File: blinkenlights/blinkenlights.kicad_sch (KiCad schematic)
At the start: 9 parts, among them U101 ATF22V10C, U102 SST39SF020, U103 SST39SF020

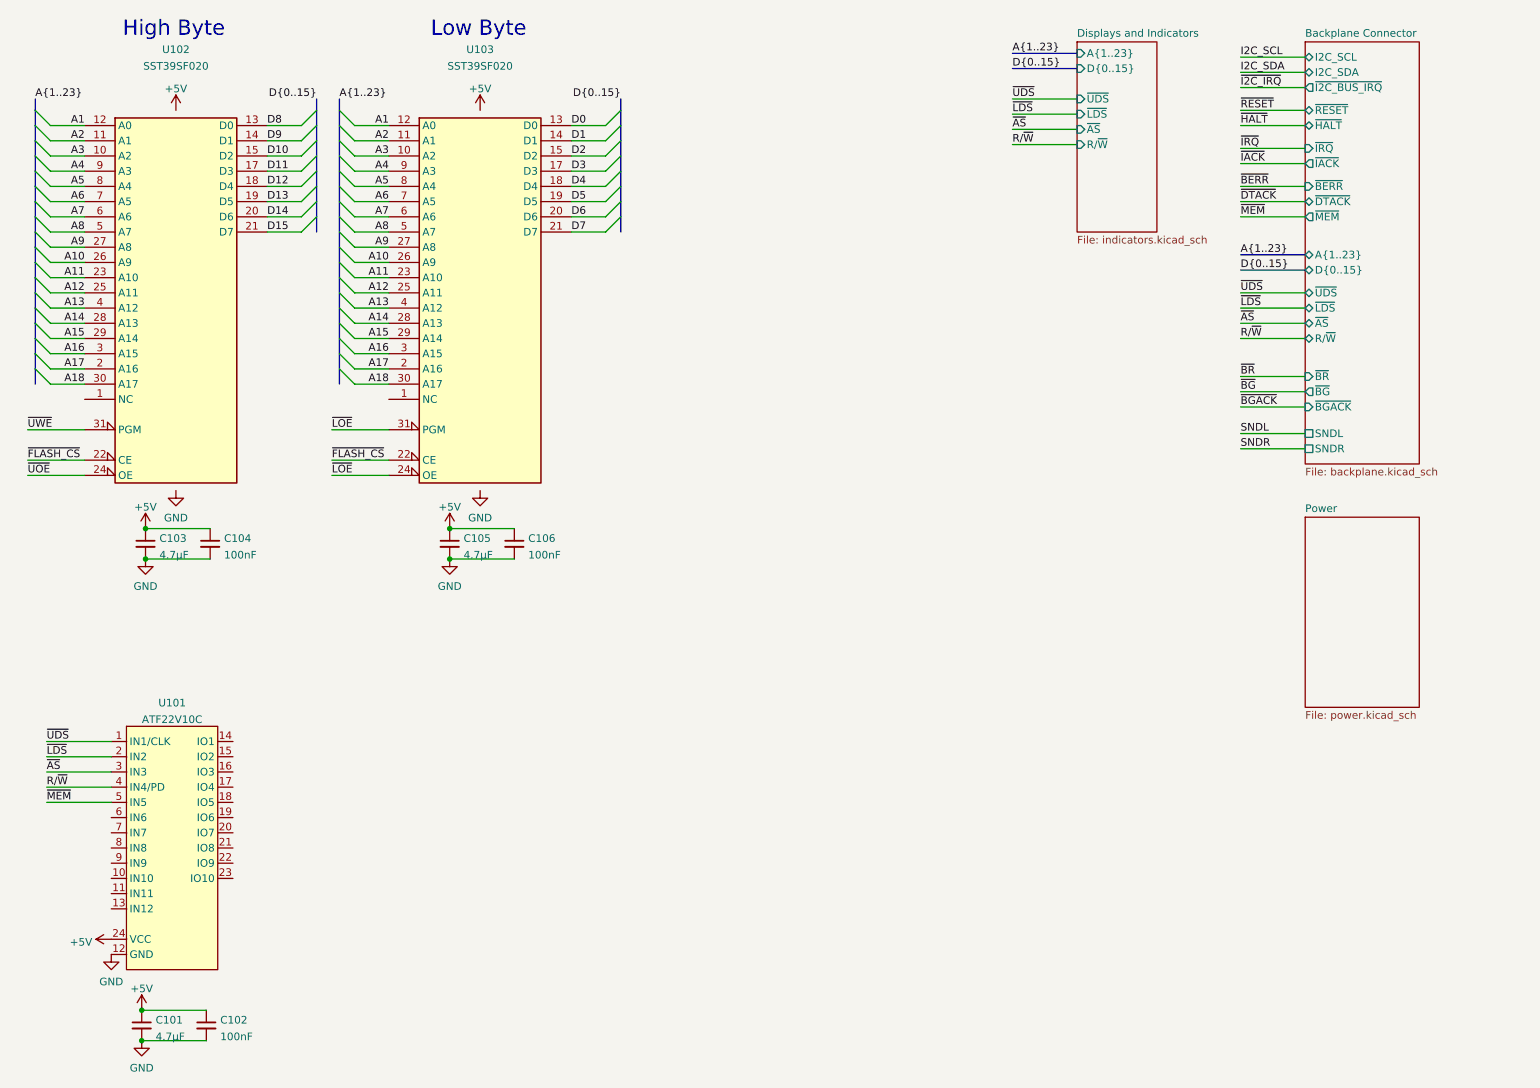
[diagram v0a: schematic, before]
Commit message: Start work on blinkenlights pcb
- This is mostly for the general layout and physical size of the board;
  all the components are placed on the back so the pin numbers will line
  up properly on the DIN connectors.
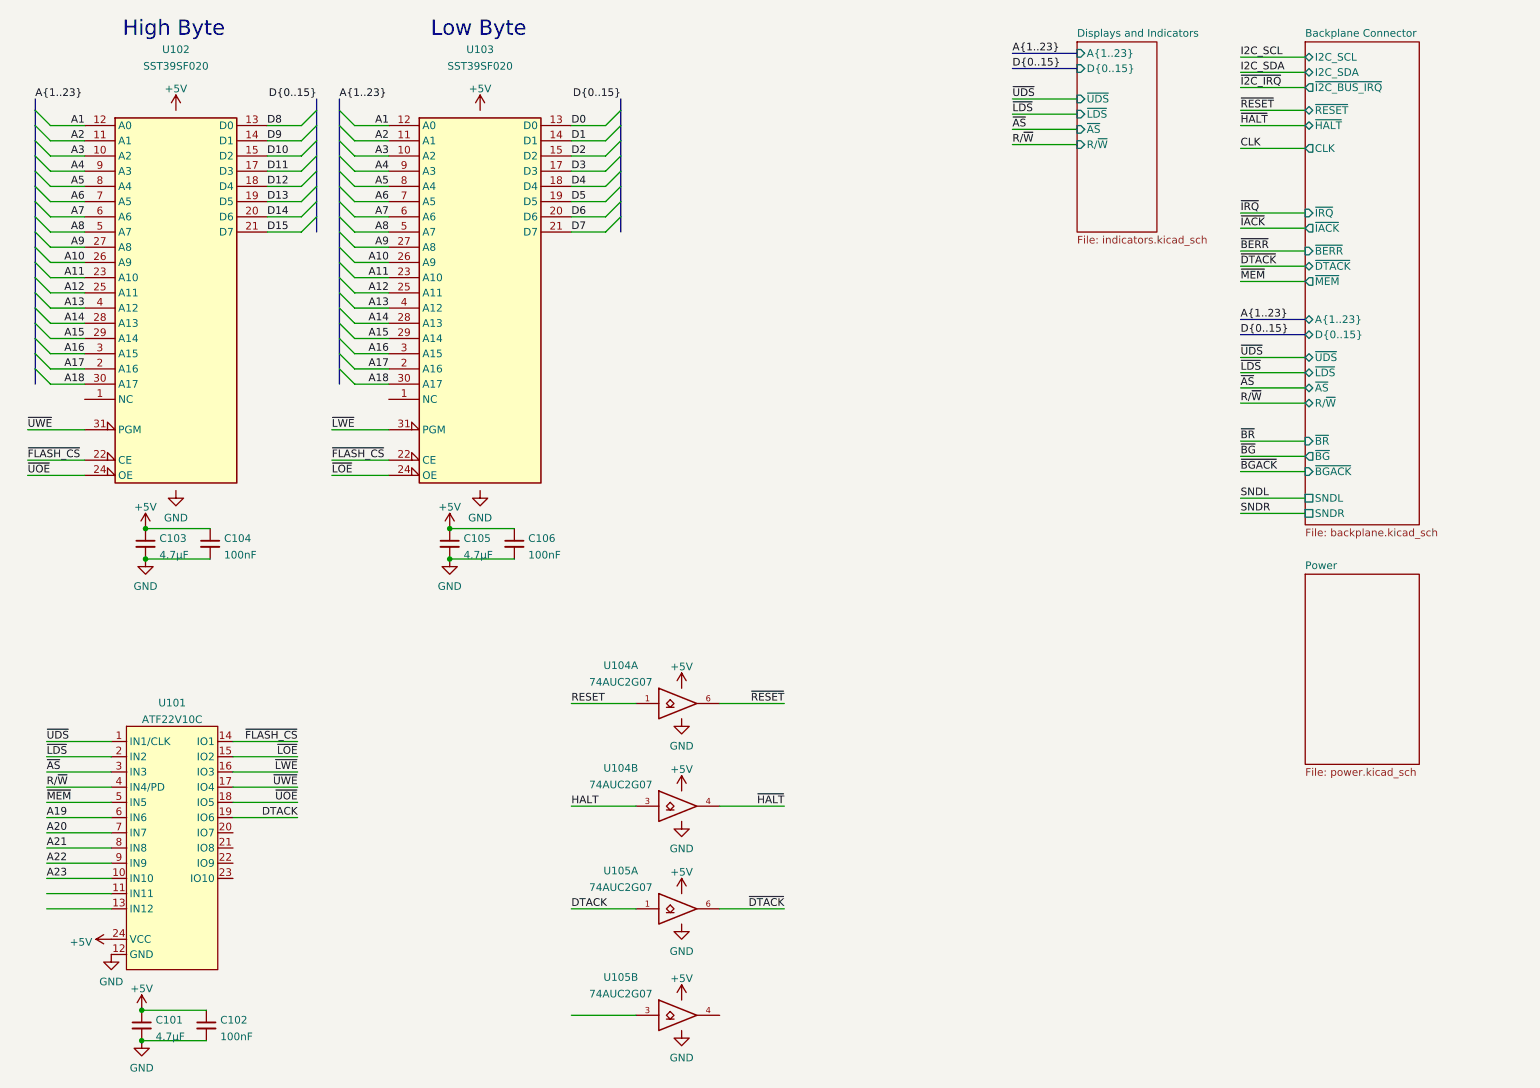
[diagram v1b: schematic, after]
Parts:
- added U104, U105: 74AUC2G07, symbol 74xGxx:74AUC2G07
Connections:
- net +5V: now also U104.5 (VCC), U104.5 (VCC), U105.5 (VCC), U105.5 (VCC)
- net GND: now also U104.2 (GND), U104.2 (GND), U105.2 (GND), U105.2 (GND)
- net ~{DTACK}: now also U105.6
- net ~{FLASH_CS}: now also U101.14 (IO1)
- net ~{HALT}: now also U104.4
- net ~{LOE}: now also U101.15 (IO2); no longer U103.31 (PGM)
- net ~{RESET}: now also U104.6
- net ~{UOE}: now also U101.18 (IO5)
- net ~{UWE}: now also U101.17 (IO4)
- net A23: now reaches U101.10 (IN10)
- net ~{LWE}: now reaches U101.16 (IO3)
- net ~{LWE}: now also U103.31 (PGM)
- net DTACK: now reaches U101.19 (IO6)
- net DTACK: now also U105.1
- net A19: now reaches U101.6 (IN6)
- net A20: now reaches U101.7 (IN7)
- net A21: now reaches U101.8 (IN8)
- net A22: now reaches U101.9 (IN9)
- new net HALT: U104.3
- new net RESET: U104.1
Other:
- sheet Backplane Connector ports: added CLK; removed none

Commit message: Added ROM sockets to blinkenlights
- Also started routing some of the IOs and powers for the displays
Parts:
- U102, U103: footprint (none) -> Socket:DIP_Socket-32_W11.9_W12.7_W15.24_W17.78_W18.5_3M_232-1285-00-0602J
- U104, U105: footprint (none) -> Package_TO_SOT_SMD:SOT-23-6
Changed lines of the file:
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@@
-(kicad_sch (version 20210621) (generator eeschema)
+(kicad_sch (version 20211123) (generator eeschema)
   (paper "A4")
-  (junction (at 40.64 185.8495) (diameter 0) (color 0 0 0 0))
-  (junction (at 41.275 100.33) (diameter 0) (color 0 0 0 0))
-  (junction (at 92.075 100.33) (diameter 0) (color 0 0 0 0))
-  (junction (at 40.64 180.7695) (diameter 0) (color 0 0 0 0))
-  (junction (at 92.075 105.41) (diameter 0) (color 0 0 0 0))
-  (junction (at 41.275 105.41) (diameter 0) (color 0 0 0 0))
+  (junction (at 92.075 100.33) (diameter 0) (color 0 0 0 0)
+  )
+  (junction (at 41.275 105.41) (diameter 0) (color 0 0 0 0)
+  )
+  (junction (at 92.075 105.41) (diameter 0) (color 0 0 0 0)
+  )
+  (junction (at 40.64 185.8495) (diameter 0) (color 0 0 0 0)
+  )
+  (junction (at 41.275 100.33) (diameter 0) (color 0 0 0 0)
+  )
+  (junction (at 40.64 180.7695) (diameter 0) (color 0 0 0 0)
+  )
   (bus_entry (at 22.86 55.88) (size 2.54 2.54)
     (stroke (width 0) (type default) (color 0 0 0 0))
@@
     (property "Reference" "U102" (id 0) (at 46.355 20.32 0))
     (property "Value" "SST39SF020" (id 1) (at 46.355 23.0951 0))
-    (property "Footprint" "" (id 2) (at 46.355 55.88 0)
+    (property "Footprint" "Socket:DIP_Socket-32_W11.9_W12.7_W15.24_W17.78_W18.5_3M_232-1285-00-0602J" (id 2) (at 46.355 55.88 0)
       (effects (font (size 1.27 1.27)) hide)
     )
@@
     (property "Reference" "U105" (id 0) (at 120.65 175.26 0))
     (property "Value" "74AUC2G07" (id 1) (at 120.65 178.0351 0))
-    (property "Footprint" "" (id 2) (at 130.81 181.61 0)
+    (property "Footprint" "Package_TO_SOT_SMD:SOT-23-6" (id 2) (at 130.81 181.61 0)
       (effects (font (size 1.27 1.27)) hide)
     )
@@
     (property "Reference" "U104" (id 0) (at 120.65 123.19 0))
     (property "Value" "74AUC2G07" (id 1) (at 120.65 125.9651 0))
-    (property "Footprint" "" (id 2) (at 130.81 129.54 0)
+    (property "Footprint" "Package_TO_SOT_SMD:SOT-23-6" (id 2) (at 130.81 129.54 0)
       (effects (font (size 1.27 1.27)) hide)
     )
@@
     (property "Reference" "U104" (id 0) (at 120.65 140.335 0))
     (property "Value" "74AUC2G07" (id 1) (at 120.65 143.1101 0))
-    (property "Footprint" "" (id 2) (at 130.81 146.685 0)
+    (property "Footprint" "Package_TO_SOT_SMD:SOT-23-6" (id 2) (at 130.81 146.685 0)
       (effects (font (size 1.27 1.27)) hide)
     )
@@
     (property "Reference" "U105" (id 0) (at 120.65 157.48 0))
     (property "Value" "74AUC2G07" (id 1) (at 120.65 160.2551 0))
-    (property "Footprint" "" (id 2) (at 130.81 163.83 0)
+    (property "Footprint" "Package_TO_SOT_SMD:SOT-23-6" (id 2) (at 130.81 163.83 0)
       (effects (font (size 1.27 1.27)) hide)
     )
@@
     (property "Reference" "U103" (id 0) (at 97.155 20.32 0))
     (property "Value" "SST39SF020" (id 1) (at 97.155 23.0951 0))
-    (property "Footprint" "" (id 2) (at 97.155 55.88 0)
+    (property "Footprint" "Socket:DIP_Socket-32_W11.9_W12.7_W15.24_W17.78_W18.5_3M_232-1285-00-0602J" (id 2) (at 97.155 55.88 0)
       (effects (font (size 1.27 1.27)) hide)
     )
@@
     )
     (path "/3d731778-a5af-4f9e-811c-c871f6087065"
-      (reference "U102") (unit 1) (value "SST39SF020") (footprint "")
+      (reference "U102") (unit 1) (value "SST39SF020") (footprint "Socket:DIP_Socket-32_W11.9_W12.7_W15.24_W17.78_W18.5_3M_232-1285-00-0602J")
     )
     (path "/dc238c24-921d-4ba3-8f23-bfce9f1710e4"
-      (reference "U103") (unit 1) (value "SST39SF020") (footprint "")
+      (reference "U103") (unit 1) (value "SST39SF020") (footprint "Socket:DIP_Socket-32_W11.9_W12.7_W15.24_W17.78_W18.5_3M_232-1285-00-0602J")
     )
     (path "/7be4bb3b-0039-4ab4-b9ab-db494a5436c4"
-      (reference "U104") (unit 1) (value "74AUC2G07") (footprint "")
+      (reference "U104") (unit 1) (value "74AUC2G07") (footprint "Package_TO_SOT_SMD:SOT-23-6")
     )
     (path "/a2030f51-0e9e-4bb0-a2a6-6ec843311267"
-      (reference "U104") (unit 2) (value "74AUC2G07") (footprint "")
+      (reference "U104") (unit 2) (value "74AUC2G07") (footprint "Package_TO_SOT_SMD:SOT-23-6")
     )
     (path "/cc4cad9f-eee2-4f14-b752-e2ae4978da88"
-      (reference "U105") (unit 1) (value "74AUC2G07") (footprint "")
+      (reference "U105") (unit 1) (value "74AUC2G07") (footprint "Package_TO_SOT_SMD:SOT-23-6")
     )
     (path "/5b533f28-f2ee-479a-8d78-ccb2fc69f1c8"
-      (reference "U105") (unit 2) (value "74AUC2G07") (footprint "")
+      (reference "U105") (unit 2) (value "74AUC2G07") (footprint "Package_TO_SOT_SMD:SOT-23-6")
     )
     (path "/ac27a395-2840-4b7c-b1d6-4dd5b3756890/6472f6b3-7e24-4f20-b2ca-c4dfaa8e4aac"
@@
     )
     (path "/38d32164-31d5-4dda-bbb2-5564054445bc/39f3650d-4670-470b-a3af-c34048ece6c9"
-      (reference "U401") (unit 1) (value "74HC244") (footprint "")
-    )
-  )
+      (reference "U401") (unit 1) (value "74HC244") (footprint "Package_SO:TSSOP-20_4.4x6.5mm_P0.65mm")
+    )
+  )

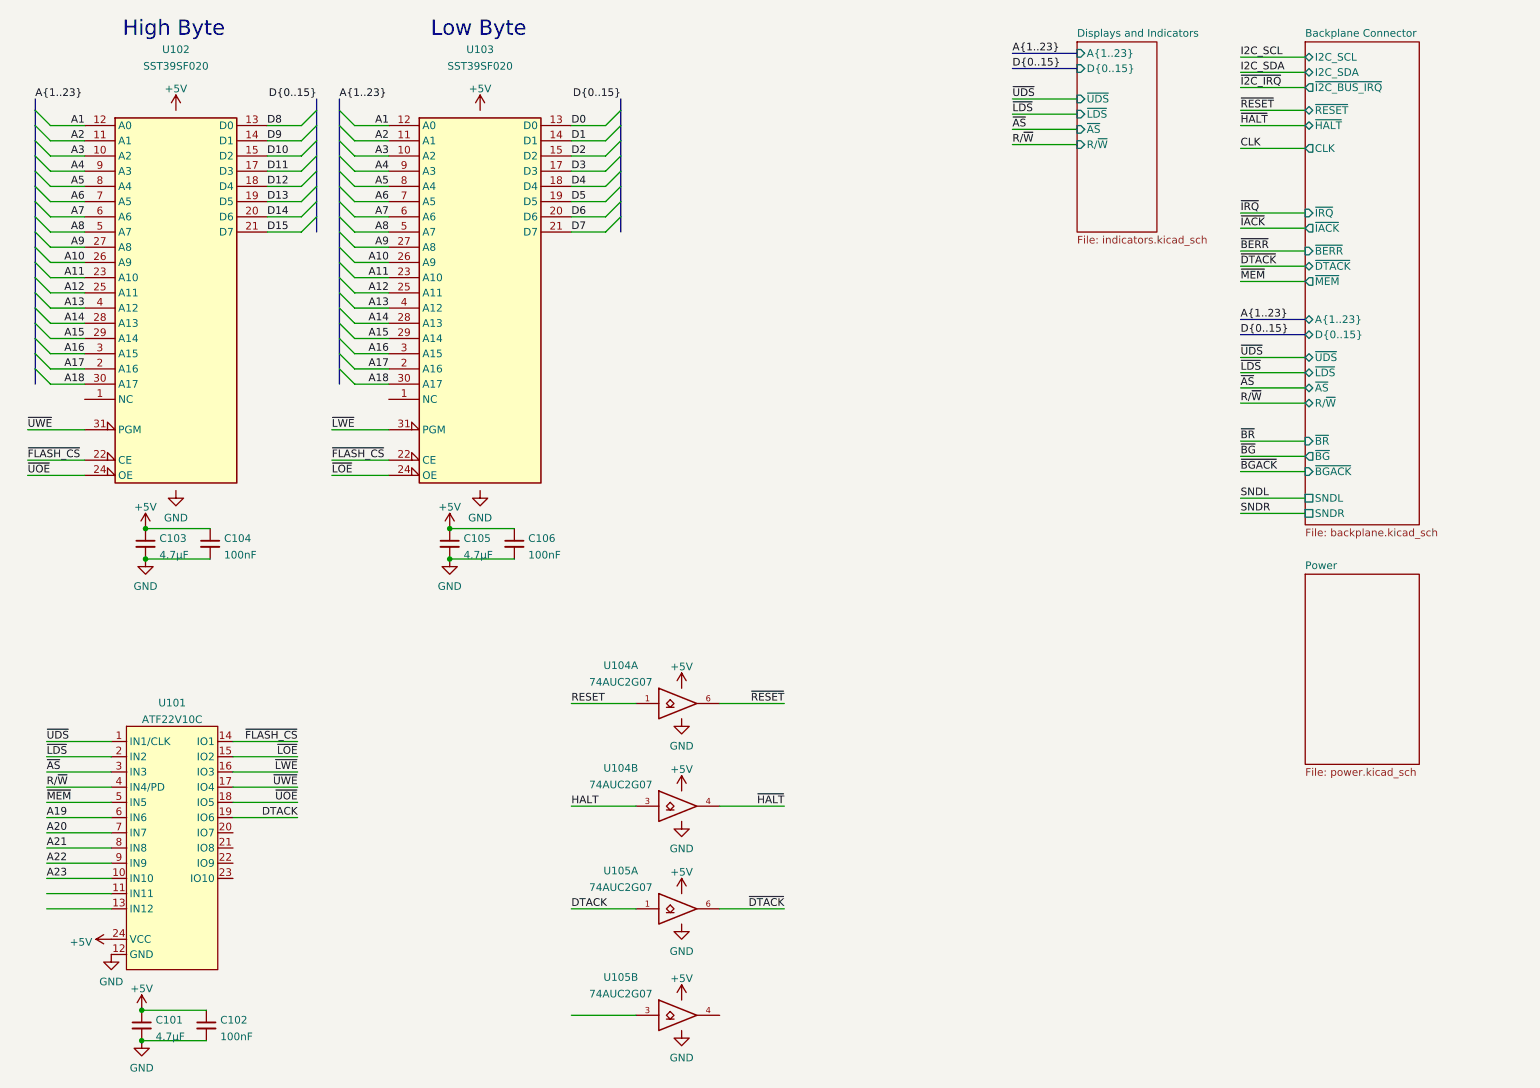
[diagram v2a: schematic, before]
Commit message: Reworked blinkenlights board
- The connector for the CPU board is a female vertical DIN connector
  instead now, which will be a lot less fucky

- Some more LEDs and buttons
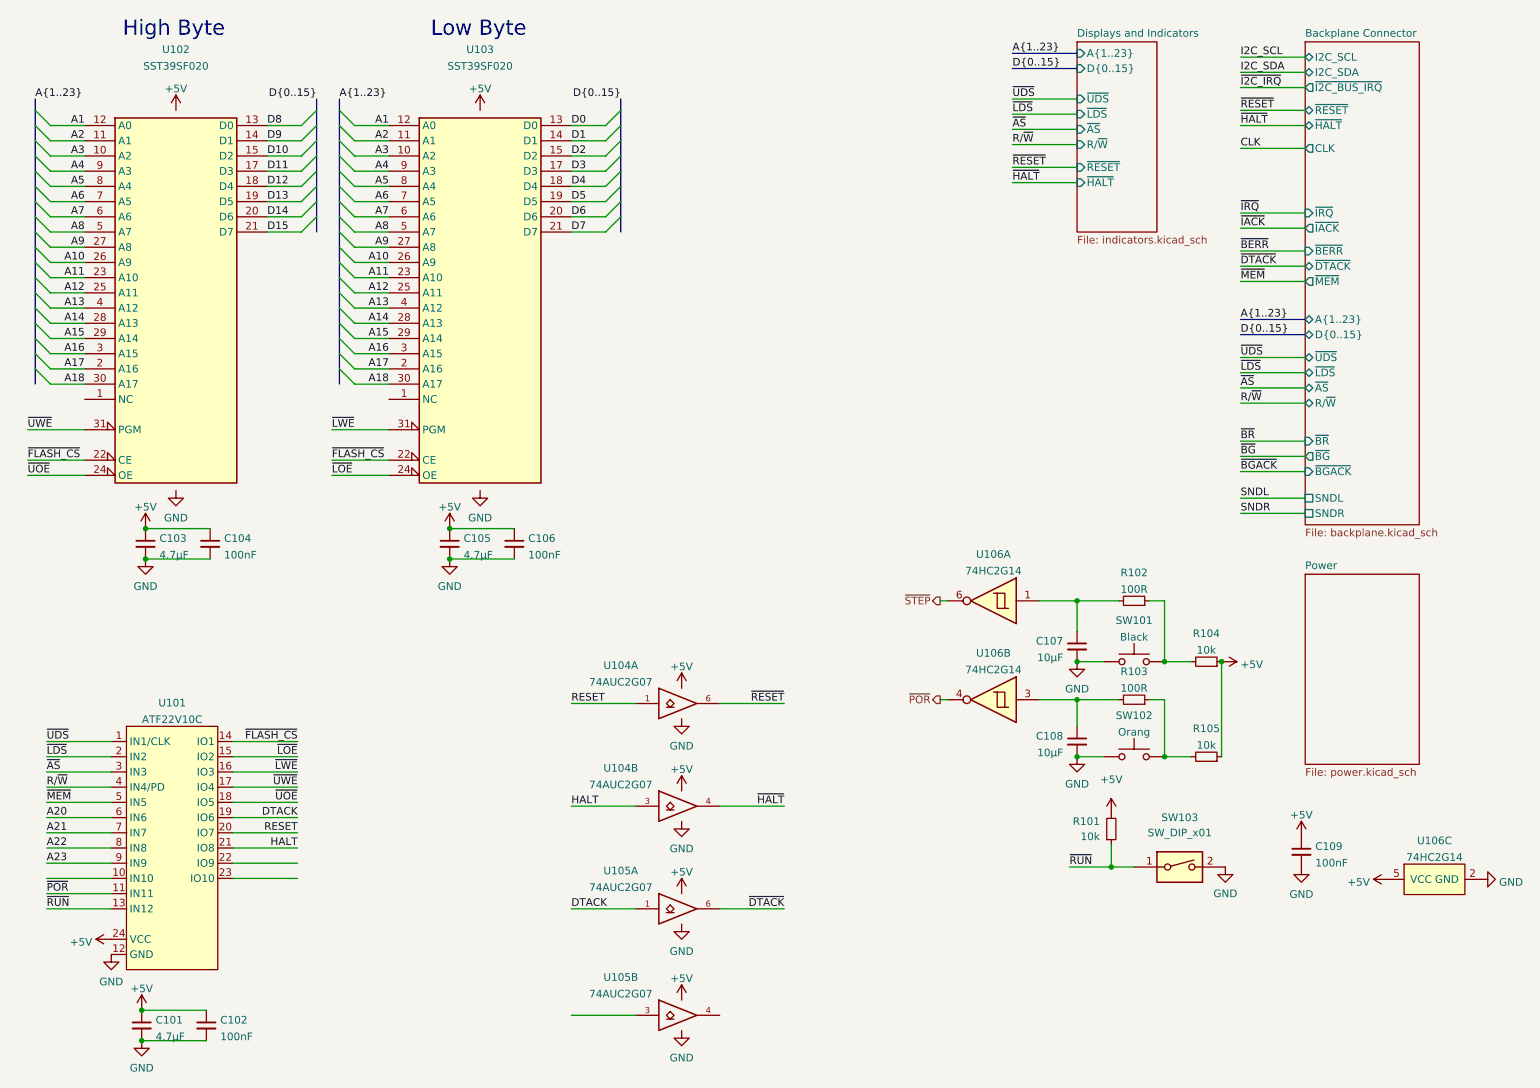
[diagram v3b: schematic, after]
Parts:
- added C107, C108: 10µF, Capacitor_SMD:C_0805_2012Metric, symbol Device:C_Small
- added C109: 100nF, Capacitor_SMD:C_0805_2012Metric, symbol Device:C_Small
- added R101, R104, R105: 10k, Resistor_SMD:R_0805_2012Metric, symbol Device:R_Small
- added R102, R103: 100R, Resistor_SMD:R_0805_2012Metric, symbol Device:R_Small
- added SW101: Black, Button_Switch_THT:SW_TH_Tactile_Omron_B3F-10xx, symbol Switch:SW_Push
- added SW102: Orang, Button_Switch_THT:SW_TH_Tactile_Omron_B3F-10xx, symbol Switch:SW_Push
- added SW103: SW_DIP_x01, Button_Switch_THT:SW_DIP_SPSTx01_Slide_9.78x4.72mm_W7.62mm_P2.54mm, symbol Switch:SW_DIP_x01
- added U106: 74HC2G14, Package_SO:TSOP-6_1.65x3.05mm_P0.95mm, symbol 68komputer-common:74HC2G14
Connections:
- net A19 is gone; now on net A20: U101.6 (IN6)
- net +5V: now also C109.1, R101.2, R104.1, R105.1, U106.5 (VCC)
- net A20: no longer U101.7 (IN7)
- net A21: now also U101.7 (IN7); no longer U101.8 (IN8)
- net A22: now also U101.8 (IN8); no longer U101.9 (IN9)
- net A23: now also U101.9 (IN9); no longer U101.10 (IN10)
- net GND: now also C107.2, C108.2, C109.2, SW101.1, SW102.1, SW103.2, U106.2 (GND)
- net HALT: now also U101.21 (IO8)
- net RESET: now also U101.20 (IO7)
- net ~{POR}: now reaches U101.11 (IN11)
- net ~{POR}: now also U106.4
- net ~{RUN}: now reaches U101.13 (IN12)
- net ~{RUN}: now also R101.1, SW103.1
- new net: R103.1, R105.2, SW102.2
- new net: C108.1, R103.2, U106.3
- new net: C107.1, R102.2, U106.1
- new net: R102.1, R104.2, SW101.2
- new net ~{STEP}: U106.6
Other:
- sheet Displays and Indicators ports: added ~{HALT}, ~{RESET}; removed none
